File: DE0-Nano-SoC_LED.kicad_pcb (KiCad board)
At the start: 2 copper layers, 96.8 x 178.3 mm, 70 parts, among them J1 Conn_02x08_Odd_Even, J10 Conn_01x08, J11 Conn_01x01, J12 Conn_01x01, J13 Conn_01x01, J14 Conn_01x01, J15 Conn_01x01, J16 Conn_01x10, J17 Conn_01x08, J18 Conn_01x01, J19 Conn_01x01, J2 Conn_02x08_Odd_Even, J3 Conn_02x20_Odd_Even, J4 Conn_02x20_Odd_Even, J5 Conn_02x08_Odd_Even, J6 Conn_02x08_Odd_Even, J7 Conn_02x08_Odd_Even, J8 Conn_01x01, J9 Conn_01x06, U1 74HC245, U10 74HC245, U2 74HC245, U3 74HC245, U4 74HC245, U5 74HC245, U6 74HC245, U7 74HC245, U8 74HC245, U9 74HC245

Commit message: pin rename
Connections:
- J4 pad 1: /G1_10 -> /G1_6
- J4 pad 10: /R2_9 -> /R2_7
- J4 pad 13: /G2_9 -> /G2_7
- J4 pad 14: /B2_9 -> /B2_7
- J4 pad 2: /B1_10 -> /B1_6
- J4 pad 27: /B1_7 -> /B1_9
- J4 pad 28: /G1_7 -> /G1_9
- J4 pad 3: /R1_10 -> /R1_6
- J4 pad 31: /R2_7 -> /R2_9
- J4 pad 32: /R1_7 -> /R1_9
- J4 pad 33: /B2_7 -> /B2_9
- J4 pad 34: /G2_7 -> /G2_9
- J4 pad 35: /B1_6 -> /B1_10
- J4 pad 36: /G1_6 -> /G1_10
- J4 pad 37: /G2_6 -> /G2_10
- J4 pad 38: /R1_6 -> /R1_10
- J4 pad 39: /B2_6 -> /B2_10
- J4 pad 4: /R2_10 -> /R2_6
- J4 pad 40: /R2_6 -> /R2_10
- J4 pad 5: /G2_10 -> /G2_6
- J4 pad 6: /B2_10 -> /B2_6
- J4 pad 7: /G1_9 -> /G1_7
- J4 pad 8: /B1_9 -> /B1_7
- J4 pad 9: /R1_9 -> /R1_7
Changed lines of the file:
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@@
     (links 350)
     (no_connects 1)
-    (area 9.994999 14.94 174.71 196.940001)
+    (area 66.414999 16.754999 163.235001 195.055001)
     (thickness 1.6)
     (drawings 39)
@@
     )
     (pad 1 thru_hole rect (at 0 0 270) (size 1.7 1.7) (drill 1) (layers *.Cu *.Mask)
-      (net 201 /G1_10))
+      (net 233 /G1_6))
     (pad 2 thru_hole oval (at 2.54 0 270) (size 1.7 1.7) (drill 1) (layers *.Cu *.Mask)
-      (net 202 /B1_10))
+      (net 232 /B1_6))
     (pad 3 thru_hole oval (at 0 2.54 270) (size 1.7 1.7) (drill 1) (layers *.Cu *.Mask)
-      (net 203 /R1_10))
+      (net 235 /R1_6))
     (pad 4 thru_hole oval (at 2.54 2.54 270) (size 1.7 1.7) (drill 1) (layers *.Cu *.Mask)
-      (net 204 /R2_10))
+      (net 237 /R2_6))
     (pad 5 thru_hole oval (at 0 5.08 270) (size 1.7 1.7) (drill 1) (layers *.Cu *.Mask)
-      (net 205 /G2_10))
+      (net 234 /G2_6))
     (pad 6 thru_hole oval (at 2.54 5.08 270) (size 1.7 1.7) (drill 1) (layers *.Cu *.Mask)
-      (net 206 /B2_10))
+      (net 236 /B2_6))
     (pad 7 thru_hole oval (at 0 7.62 270) (size 1.7 1.7) (drill 1) (layers *.Cu *.Mask)
-      (net 207 /G1_9))
+      (net 226 /G1_7))
     (pad 8 thru_hole oval (at 2.54 7.62 270) (size 1.7 1.7) (drill 1) (layers *.Cu *.Mask)
-      (net 208 /B1_9))
+      (net 225 /B1_7))
     (pad 9 thru_hole oval (at 0 10.16 270) (size 1.7 1.7) (drill 1) (layers *.Cu *.Mask)
-      (net 209 /R1_9))
+      (net 229 /R1_7))
     (pad 10 thru_hole oval (at 2.54 10.16 270) (size 1.7 1.7) (drill 1) (layers *.Cu *.Mask)
-      (net 210 /R2_9))
+      (net 228 /R2_7))
     (pad 11 thru_hole oval (at 0 12.7 270) (size 1.7 1.7) (drill 1) (layers *.Cu *.Mask)
       (net 3 VCC))
@@
       (net 1 GND))
     (pad 13 thru_hole oval (at 0 15.24 270) (size 1.7 1.7) (drill 1) (layers *.Cu *.Mask)
-      (net 211 /G2_9))
+      (net 231 /G2_7))
     (pad 14 thru_hole oval (at 2.54 15.24 270) (size 1.7 1.7) (drill 1) (layers *.Cu *.Mask)
-      (net 212 /B2_9))
+      (net 230 /B2_7))
     (pad 15 thru_hole oval (at 0 17.78 270) (size 1.7 1.7) (drill 1) (layers *.Cu *.Mask)
       (net 213 /CLK__2))
@@
       (net 224 /G2_8))
     (pad 27 thru_hole oval (at 0 33.02 270) (size 1.7 1.7) (drill 1) (layers *.Cu *.Mask)
-      (net 225 /B1_7))
+      (net 208 /B1_9))
     (pad 28 thru_hole oval (at 2.54 33.02 270) (size 1.7 1.7) (drill 1) (layers *.Cu *.Mask)
-      (net 226 /G1_7))
+      (net 207 /G1_9))
     (pad 29 thru_hole oval (at 0 35.56 270) (size 1.7 1.7) (drill 1) (layers *.Cu *.Mask)
       (net 227 /3V3))
@@
       (net 1 GND))
     (pad 31 thru_hole oval (at 0 38.1 270) (size 1.7 1.7) (drill 1) (layers *.Cu *.Mask)
-      (net 228 /R2_7))
+      (net 210 /R2_9))
     (pad 32 thru_hole oval (at 2.54 38.1 270) (size 1.7 1.7) (drill 1) (layers *.Cu *.Mask)
-      (net 229 /R1_7))
+      (net 209 /R1_9))
     (pad 33 thru_hole oval (at 0 40.64 270) (size 1.7 1.7) (drill 1) (layers *.Cu *.Mask)
-      (net 230 /B2_7))
+      (net 212 /B2_9))
     (pad 34 thru_hole oval (at 2.54 40.64 270) (size 1.7 1.7) (drill 1) (layers *.Cu *.Mask)
-      (net 231 /G2_7))
+      (net 211 /G2_9))
     (pad 35 thru_hole oval (at 0 43.18 270) (size 1.7 1.7) (drill 1) (layers *.Cu *.Mask)
-      (net 232 /B1_6))
+      (net 202 /B1_10))
     (pad 36 thru_hole oval (at 2.54 43.18 270) (size 1.7 1.7) (drill 1) (layers *.Cu *.Mask)
-      (net 233 /G1_6))
+      (net 201 /G1_10))
     (pad 37 thru_hole oval (at 0 45.72 270) (size 1.7 1.7) (drill 1) (layers *.Cu *.Mask)
-      (net 234 /G2_6))
+      (net 205 /G2_10))
     (pad 38 thru_hole oval (at 2.54 45.72 270) (size 1.7 1.7) (drill 1) (layers *.Cu *.Mask)
-      (net 235 /R1_6))
+      (net 203 /R1_10))
     (pad 39 thru_hole oval (at 0 48.26 270) (size 1.7 1.7) (drill 1) (layers *.Cu *.Mask)
-      (net 236 /B2_6))
+      (net 206 /B2_10))
     (pad 40 thru_hole oval (at 2.54 48.26 270) (size 1.7 1.7) (drill 1) (layers *.Cu *.Mask)
-      (net 237 /R2_6))
+      (net 204 /R2_10))
     (model ${KISYS3DMOD}/Pin_Headers.3dshapes/Pin_Header_Straight_2x20_Pitch2.54mm.wrl
       (at (xyz 0 0 0))

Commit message: almost all components
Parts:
- added J20, J21, J22, J23, J24: Conn_02x08_Odd_Even, Connectors_Multicomp:Multicomp_MC9A12-1634_2x08x2.54mm_Straight, F.Cu at (114.8, 205.1)
- added RN21, RN22, RN23, RN24, RN25, RN26, RN27, RN28, RN29, RN30, RN31, RN32, RN33, RN34, RN35, RN36, RN37, RN38, RN39, RN40: R_Pack04, Resistors_SMD:R_Array_Concave_4x0402, F.Cu at (114.8, 205.1)
- added U11, U12, U13, U14, U15, U16, U17, U18, U19, U20: 74HC245, SMD_Packages:SSOP-20, F.Cu at (114.8, 205.1)

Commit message: pin rename
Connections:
- J20 pad 1: /R1_1_1 -> /R1_10_2
- J20 pad 10: /B_1_1 -> /B_10_2
- J20 pad 11: /C_1_1 -> /C_10_2
- J20 pad 12: /D_1_1 -> /D_10_2
- J20 pad 13: /CLK_1_1 -> /CLK_10_2
- J20 pad 14: /LAT_1_1 -> /LAT_10_2
- J20 pad 15: /OE_1_1 -> /OE_10_2
- J20 pad 2: /G1_1_1 -> /G1_10_2
- J20 pad 3: /B1_1_1 -> /B1_10_2
- J20 pad 5: /R2_1_1 -> /R2_10_2
- J20 pad 6: /G2_1_1 -> /G2_10_2
- J20 pad 7: /B2_1_1 -> /B2_10_2
- J20 pad 9: /A_1_1 -> /A_10_2
- J21 pad 1: /R1_2_1 -> /R1_9_2
- J21 pad 10: /B_2_1 -> /B_9_2
- J21 pad 11: /C_2_1 -> /C_9_2
- J21 pad 12: /D_2_1 -> /D_9_2
- J21 pad 13: /CLK_2_1 -> /CLK_9_2
- J21 pad 14: /LAT_2_1 -> /LAT_9_2
- J21 pad 15: /OE_2_1 -> /OE_9_2
- J21 pad 2: /G1_2_1 -> /G1_9_2
- J21 pad 3: /B1_2_1 -> /B1_9_2
- J21 pad 5: /R2_2_1 -> /R2_9_2
- J21 pad 6: /G2_2_1 -> /G2_9_2
- J21 pad 7: /B2_2_1 -> /B2_9_2
- J21 pad 9: /A_2_1 -> /A_9_2
- J22 pad 1: /R1_3_1 -> /R1_8_2
- J22 pad 10: /B_3_1 -> /B_8_2
- J22 pad 11: /C_3_1 -> /C_8_2
- J22 pad 12: /D_3_1 -> /D_8_2
- J22 pad 13: /CLK_3_1 -> /CLK_8_2
- J22 pad 14: /LAT_3_1 -> /LAT_8_2
- J22 pad 15: /OE_3_1 -> /OE_8_2
- J22 pad 2: /G1_3_1 -> /G1_8_2
- J22 pad 3: /B1_3_1 -> /B1_8_2
- J22 pad 5: /R2_3_1 -> /R2_8_2
- J22 pad 6: /G2_3_1 -> /G2_8_2
- J22 pad 7: /B2_3_1 -> /B2_8_2
- J22 pad 9: /A_3_1 -> /A_8_2
- J23 pad 1: /R1_4_1 -> /R1_7_2
- J23 pad 10: /B_4_1 -> /B_7_2
- J23 pad 11: /C_4_1 -> /C_7_2
- J23 pad 12: /D_4_1 -> /D_7_2
- J23 pad 13: /CLK_4_1 -> /CLK_7_2
- J23 pad 14: /LAT_4_1 -> /LAT_7_2
- J23 pad 15: /OE_4_1 -> /OE_7_2
- J23 pad 2: /G1_4_1 -> /G1_7_2
- J23 pad 3: /B1_4_1 -> /B1_7_2
- J23 pad 5: /R2_4_1 -> /R2_7_2
- J23 pad 6: /G2_4_1 -> /G2_7_2
- J23 pad 7: /B2_4_1 -> /B2_7_2
- J23 pad 9: /A_4_1 -> /A_7_2
- J24 pad 1: /R1_5_1 -> /R1_6_2
- J24 pad 10: /B_5_1 -> /B_6_2
- J24 pad 11: /C_5_1 -> /C_6_2
- J24 pad 12: /D_5_1 -> /D_6_2
- J24 pad 13: /CLK_5_1 -> /CLK_6_2
- J24 pad 14: /LAT_5_1 -> /LAT_6_2
- J24 pad 15: /OE_5_1 -> /OE_6_2
- J24 pad 2: /G1_5_1 -> /G1_6_2
- J24 pad 3: /B1_5_1 -> /B1_6_2
- J24 pad 5: /R2_5_1 -> /R2_6_2
- J24 pad 6: /G2_5_1 -> /G2_6_2
- J24 pad 7: /B2_5_1 -> /B2_6_2
- J24 pad 9: /A_5_1 -> /A_6_2
- RN21 pad 1: /D__1 -> /D__2
- RN21 pad 2: /C__1 -> /C__2
- RN21 pad 3: /B__1 -> /B__2
- RN21 pad 4: /A__1 -> /A__2
- RN22 pad 2: /R2_1 -> /R2_10
- RN22 pad 3: /G2_1 -> /G2_10
- RN22 pad 4: /B2_1 -> /B2_10
- RN23 pad 3: /LAT__1 -> /LAT__2
- RN23 pad 4: /CLK__1 -> /CLK__2
- RN24 pad 1: /G1_1 -> /G1_10
- RN24 pad 2: /B1_1 -> /B1_10
- RN24 pad 3: /R1_1 -> /R1_10
- RN25 pad 1: /D__1 -> /D__2
- RN25 pad 2: /C__1 -> /C__2
- RN25 pad 3: /B__1 -> /B__2
- RN25 pad 4: /A__1 -> /A__2
- RN26 pad 2: /R2_2 -> /R2_9
- RN26 pad 3: /G2_2 -> /G2_9
- RN26 pad 4: /B2_2 -> /B2_9
- RN27 pad 3: /LAT__1 -> /LAT__2
- RN27 pad 4: /CLK__1 -> /CLK__2
- RN28 pad 1: /G1_2 -> /G1_9
- RN28 pad 2: /B1_2 -> /B1_9
- RN28 pad 3: /R1_2 -> /R1_9
- RN29 pad 1: /D__1 -> /D__2
- RN29 pad 2: /C__1 -> /C__2
- RN29 pad 3: /B__1 -> /B__2
- RN29 pad 4: /A__1 -> /A__2
- RN30 pad 2: /R2_3 -> /R2_8
- RN30 pad 3: /G2_3 -> /G2_8
- RN30 pad 4: /B2_3 -> /B2_8
- RN31 pad 3: /LAT__1 -> /LAT__2
- RN31 pad 4: /CLK__1 -> /CLK__2
- RN32 pad 1: /G1_3 -> /G1_8
- RN32 pad 2: /B1_3 -> /B1_8
- RN32 pad 3: /R1_3 -> /R1_8
- RN33 pad 1: /D__1 -> /D__2
- RN33 pad 2: /C__1 -> /C__2
- RN33 pad 3: /B__1 -> /B__2
- RN33 pad 4: /A__1 -> /A__2
- RN34 pad 2: /R2_4 -> /R2_7
- RN34 pad 3: /G2_4 -> /G2_7
- RN34 pad 4: /B2_4 -> /B2_7
- RN35 pad 3: /LAT__1 -> /LAT__2
- RN35 pad 4: /CLK__1 -> /CLK__2
- RN36 pad 1: /G1_4 -> /G1_7
- RN36 pad 2: /B1_4 -> /B1_7
- RN36 pad 3: /R1_4 -> /R1_7
- RN37 pad 1: /D__1 -> /D__2
- RN37 pad 2: /C__1 -> /C__2
- RN37 pad 3: /B__1 -> /B__2
- RN37 pad 4: /A__1 -> /A__2
- RN38 pad 2: /R2_5 -> /R2_6
- RN38 pad 3: /G2_5 -> /G2_6
- RN38 pad 4: /B2_5 -> /B2_6
- RN39 pad 3: /LAT__1 -> /LAT__2
- RN39 pad 4: /CLK__1 -> /CLK__2
- RN40 pad 1: /G1_5 -> /G1_6
- RN40 pad 2: /B1_5 -> /B1_6
- RN40 pad 3: /R1_5 -> /R1_6
- U11 pad 11: /A_1_1 -> /A_10_2
- U11 pad 12: /B_1_1 -> /B_10_2
- U11 pad 13: /C_1_1 -> /C_10_2
- U11 pad 14: /D_1_1 -> /D_10_2
- U11 pad 15: /CLK_1_1 -> /CLK_10_2
- U11 pad 16: /LAT_1_1 -> /LAT_10_2
- U11 pad 17: /OE_1_1 -> /OE_10_2
- U12 pad 11: /B2_1_1 -> /B2_10_2
- U12 pad 12: /G2_1_1 -> /G2_10_2
- U12 pad 13: /R2_1_1 -> /R2_10_2
- U12 pad 16: /R1_1_1 -> /R1_10_2
- U12 pad 17: /B1_1_1 -> /B1_10_2
- U12 pad 18: /G1_1_1 -> /G1_10_2
- U13 pad 11: /A_2_1 -> /A_9_2
- U13 pad 12: /B_2_1 -> /B_9_2
- U13 pad 13: /C_2_1 -> /C_9_2
- U13 pad 14: /D_2_1 -> /D_9_2
- U13 pad 15: /CLK_2_1 -> /CLK_9_2
- U13 pad 16: /LAT_2_1 -> /LAT_9_2
- U13 pad 17: /OE_2_1 -> /OE_9_2
- U14 pad 11: /B2_2_1 -> /B2_9_2
- U14 pad 12: /G2_2_1 -> /G2_9_2
- U14 pad 13: /R2_2_1 -> /R2_9_2
- U14 pad 16: /R1_2_1 -> /R1_9_2
- U14 pad 17: /B1_2_1 -> /B1_9_2
- U14 pad 18: /G1_2_1 -> /G1_9_2
- U15 pad 11: /A_3_1 -> /A_8_2
- U15 pad 12: /B_3_1 -> /B_8_2
- U15 pad 13: /C_3_1 -> /C_8_2
- U15 pad 14: /D_3_1 -> /D_8_2
- U15 pad 15: /CLK_3_1 -> /CLK_8_2
- U15 pad 16: /LAT_3_1 -> /LAT_8_2
- U15 pad 17: /OE_3_1 -> /OE_8_2
- U16 pad 11: /B2_3_1 -> /B2_8_2
- U16 pad 12: /G2_3_1 -> /G2_8_2
- U16 pad 13: /R2_3_1 -> /R2_8_2
- U16 pad 16: /R1_3_1 -> /R1_8_2
- U16 pad 17: /B1_3_1 -> /B1_8_2
- U16 pad 18: /G1_3_1 -> /G1_8_2
- U17 pad 11: /A_4_1 -> /A_7_2
- U17 pad 12: /B_4_1 -> /B_7_2
- U17 pad 13: /C_4_1 -> /C_7_2
- U17 pad 14: /D_4_1 -> /D_7_2
- U17 pad 15: /CLK_4_1 -> /CLK_7_2
- U17 pad 16: /LAT_4_1 -> /LAT_7_2
- U17 pad 17: /OE_4_1 -> /OE_7_2
- U18 pad 11: /B2_4_1 -> /B2_7_2
- U18 pad 12: /G2_4_1 -> /G2_7_2
- U18 pad 13: /R2_4_1 -> /R2_7_2
- U18 pad 16: /R1_4_1 -> /R1_7_2
- U18 pad 17: /B1_4_1 -> /B1_7_2
- U18 pad 18: /G1_4_1 -> /G1_7_2
- U19 pad 11: /A_5_1 -> /A_6_2
- U19 pad 12: /B_5_1 -> /B_6_2
- U19 pad 13: /C_5_1 -> /C_6_2
- U19 pad 14: /D_5_1 -> /D_6_2
- U19 pad 15: /CLK_5_1 -> /CLK_6_2
- U19 pad 16: /LAT_5_1 -> /LAT_6_2
- U19 pad 17: /OE_5_1 -> /OE_6_2
- U20 pad 11: /B2_5_1 -> /B2_6_2
- U20 pad 12: /G2_5_1 -> /G2_6_2
- U20 pad 13: /R2_5_1 -> /R2_6_2
- U20 pad 16: /R1_5_1 -> /R1_6_2
- U20 pad 17: /B1_5_1 -> /B1_6_2
- U20 pad 18: /G1_5_1 -> /G1_6_2

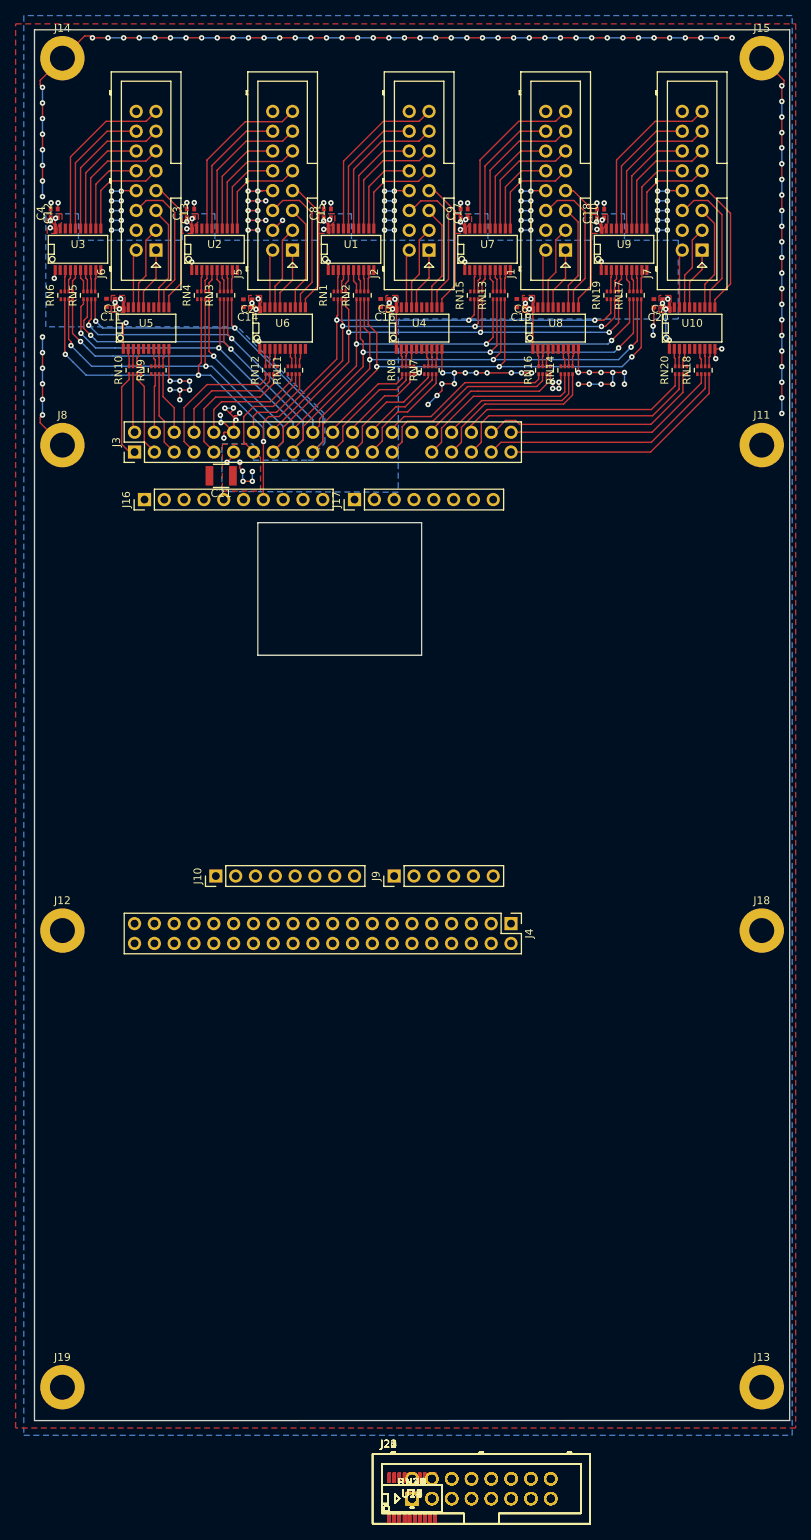
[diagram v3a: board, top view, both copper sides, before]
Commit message: small pcb fix
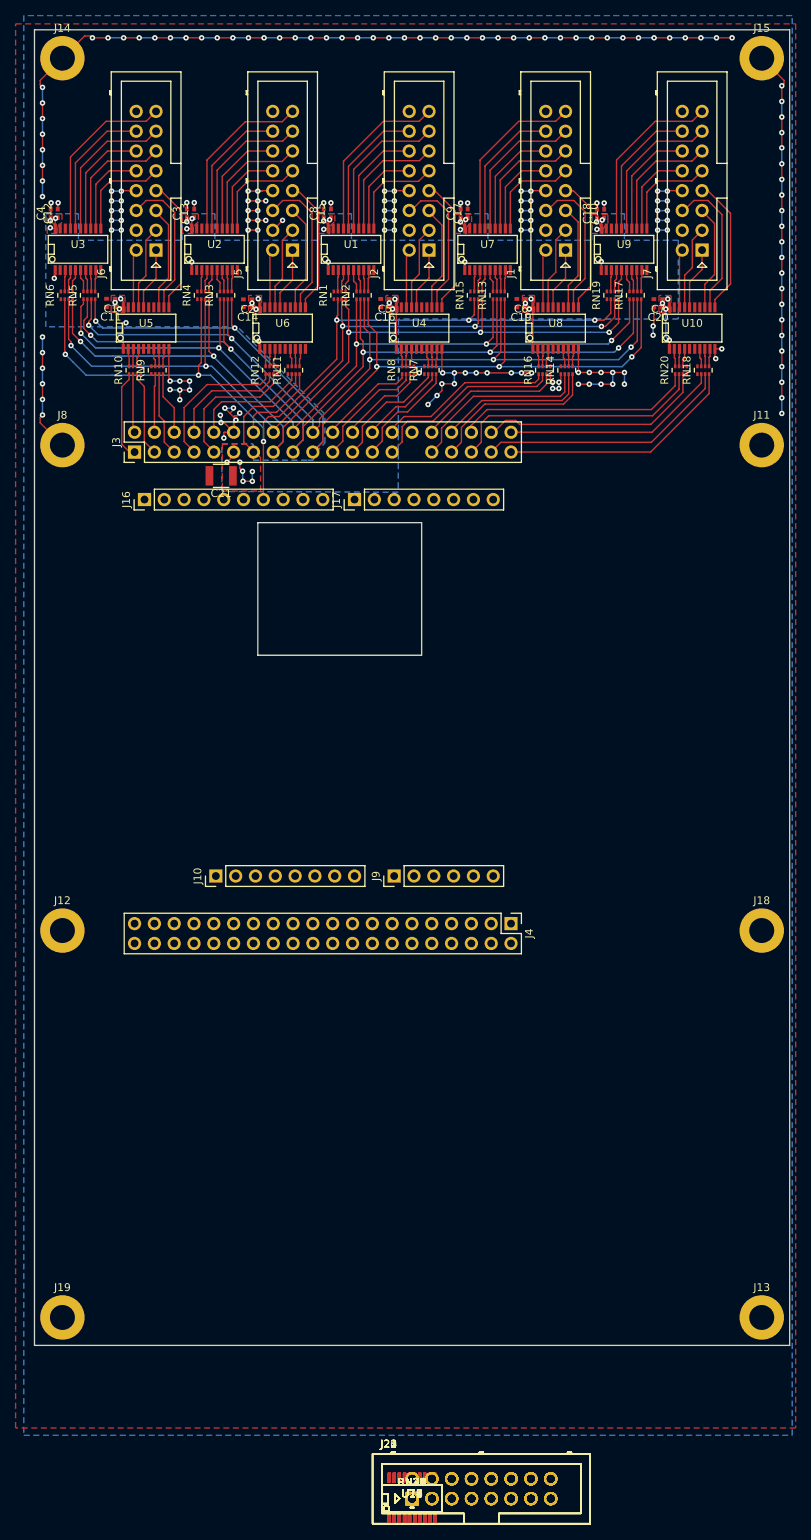
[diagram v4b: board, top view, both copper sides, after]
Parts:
- moved J13 8.94 mm to (159.7, 181.8)
- moved J19 8.94 mm to (70.0, 181.8)
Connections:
- net Net-(J10-Pad3) renamed /FPGA_AH7
- net Net-(J10-Pad8) renamed /9V
- J10 pad 2: Net-(J10-Pad2) -> /3V3
- J10 pad 4: Net-(J10-Pad4) -> /3V3
- J10 pad 5: Net-(J10-Pad5) -> VCC
- J10 pad 6: Net-(J10-Pad6) -> GND
- J10 pad 7: Net-(J10-Pad7) -> GND
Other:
- board size 96.8 x 178.3 mm -> 96.8 x 168.7 mm

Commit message: components placement continue
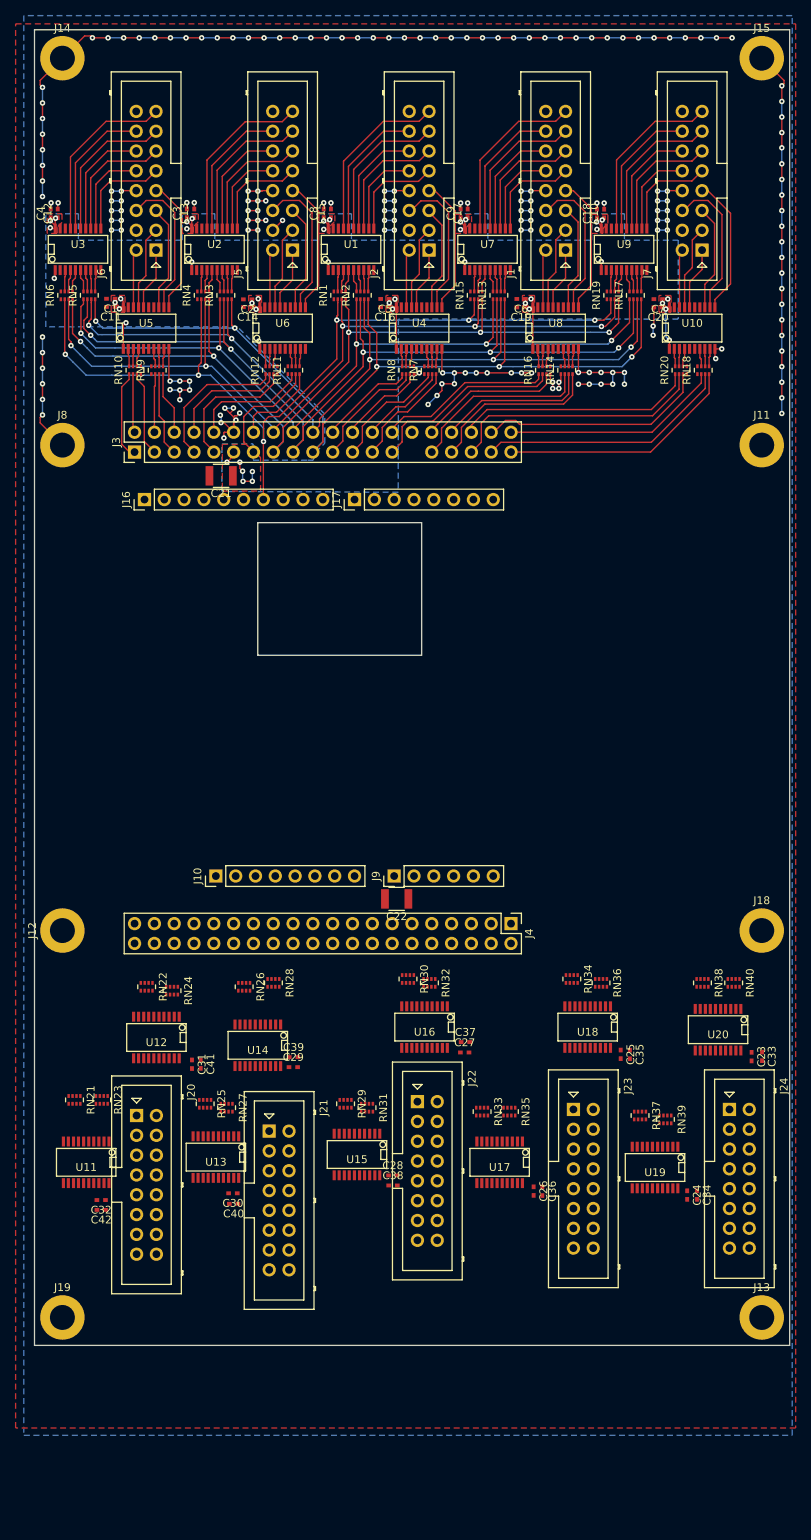
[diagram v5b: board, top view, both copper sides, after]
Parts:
- added C22: C, Capacitors_SMD:C_1210, F.Cu at (112.8, 128.2)
- added C23: 0.1, Capacitors_SMD:C_0402_NoSilk, F.Cu at (158.3, 148.4)
- added C24: 0.01, Capacitors_SMD:C_0402_NoSilk, F.Cu at (150.1, 166.1)
- added C25: 0.1, Capacitors_SMD:C_0402_NoSilk, F.Cu at (141.6, 148.1)
- added C26: 0.01, Capacitors_SMD:C_0402_NoSilk, F.Cu at (130.4, 165.6)
- added C27: 0.1, Capacitors_SMD:C_0402_NoSilk, F.Cu at (121.6, 147.9)
- added C28: 0.01, Capacitors_SMD:C_0402_NoSilk, F.Cu at (112.4, 163.6)
- added C29: 0.1, Capacitors_SMD:C_0402_NoSilk, F.Cu at (99.6, 149.7)
- added C30: 0.01, Capacitors_SMD:C_0402_NoSilk, F.Cu at (91.9, 165.9)
- added C31: 0.1, Capacitors_SMD:C_0402_NoSilk, F.Cu at (86.6, 149.4)
- added C32: 0.01, Capacitors_SMD:C_0402_NoSilk, F.Cu at (75.0, 166.8)
- added C33: 0.1, Capacitors_SMD:C_0402_NoSilk, F.Cu at (159.7, 148.4)
- added C34: 0.01, Capacitors_SMD:C_0402_NoSilk, F.Cu at (151.3, 166.1)
- added C35: 0.1, Capacitors_SMD:C_0402_NoSilk, F.Cu at (142.8, 148.1)
- added C36: 0.01, Capacitors_SMD:C_0402_NoSilk, F.Cu at (131.5, 165.7)
- added C37: 0.1, Capacitors_SMD:C_0402_NoSilk, F.Cu at (121.7, 146.5)
- added C38: 0.01, Capacitors_SMD:C_0402_NoSilk, F.Cu at (112.4, 164.9)
- added C39: 0.1, Capacitors_SMD:C_0402_NoSilk, F.Cu at (99.6, 148.5)
- added C40: 0.01, Capacitors_SMD:C_0402_NoSilk, F.Cu at (92.0, 167.3)
- added C41: 0.1, Capacitors_SMD:C_0402_NoSilk, F.Cu at (87.7, 149.3)
- added C42: 0.01, Capacitors_SMD:C_0402_NoSilk, F.Cu at (75.0, 168.0)
- moved RN40 77.9 mm to (156.1, 138.9), turned to 270 degrees
- moved RN38 75.9 mm to (152.1, 138.9), turned to 270 degrees
- moved RN22 73.9 mm to (80.8, 139.4), turned to 270 degrees
- moved RN24 72.0 mm to (84.0, 139.9), turned to 270 degrees
- moved U20 71.8 mm to (154.1, 144.9), turned to 180 degrees
- moved RN36 70.4 mm to (139.1, 138.9), turned to 270 degrees
- moved RN34 69.7 mm to (135.3, 138.4), turned to 270 degrees
- moved RN26 69.1 mm to (93.3, 139.4), turned to 270 degrees
- moved RN28 68.5 mm to (97.0, 138.9), turned to 270 degrees
- moved U12 67.6 mm to (82.0, 145.9), turned to 180 degrees
- moved RN21 67.0 mm to (71.5, 153.9), turned to 270 degrees
- moved RN30 66.6 mm to (114.3, 138.4), turned to 270 degrees
- moved RN32 66.2 mm to (117.0, 138.9), turned to 270 degrees
- moved RN23 64.8 mm to (75.0, 153.9), turned to 270 degrees
- moved U18 64.5 mm to (137.3, 144.6), turned to 180 degrees
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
